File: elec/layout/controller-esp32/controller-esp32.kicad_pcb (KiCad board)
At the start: 2 copper layers, 40 x 40 mm, 0 parts

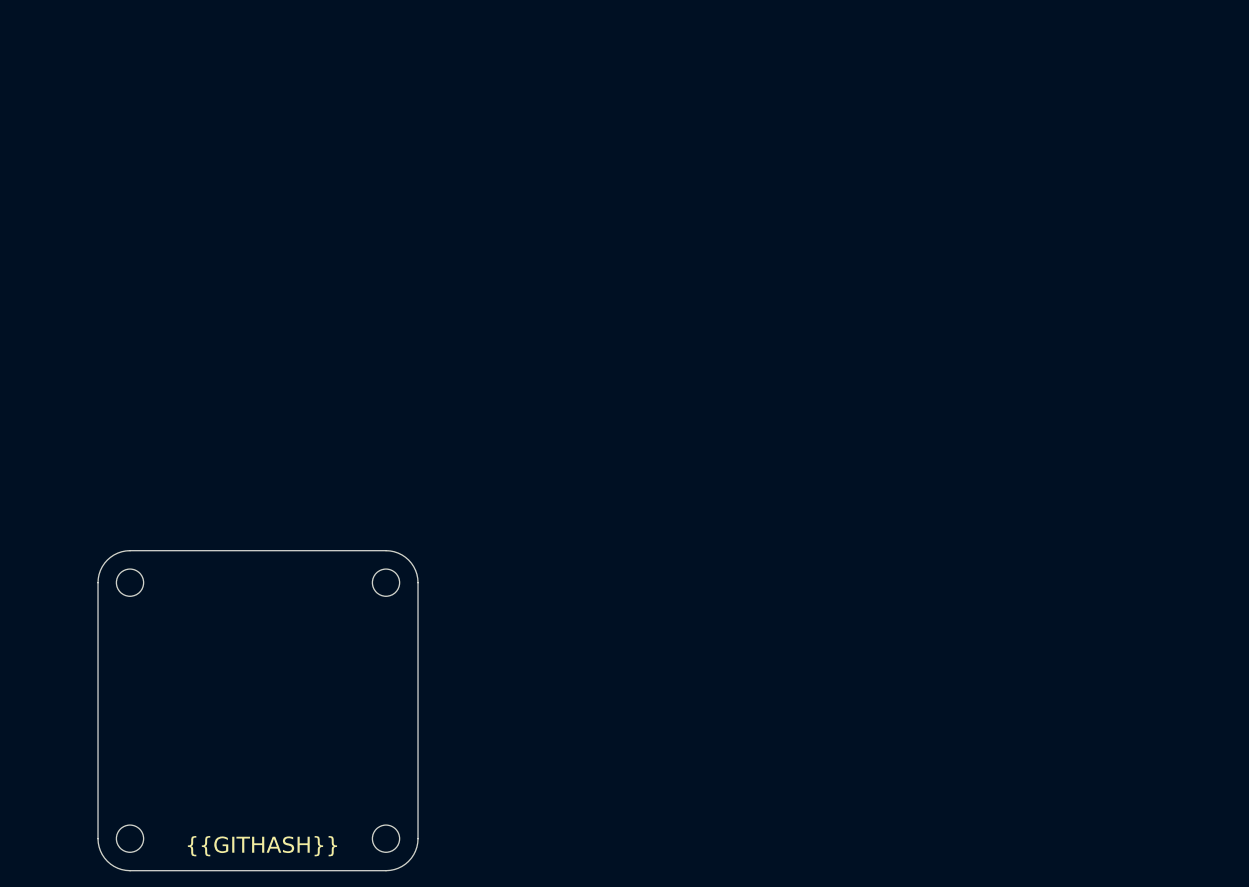
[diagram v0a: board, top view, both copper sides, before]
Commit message: Layout controller block
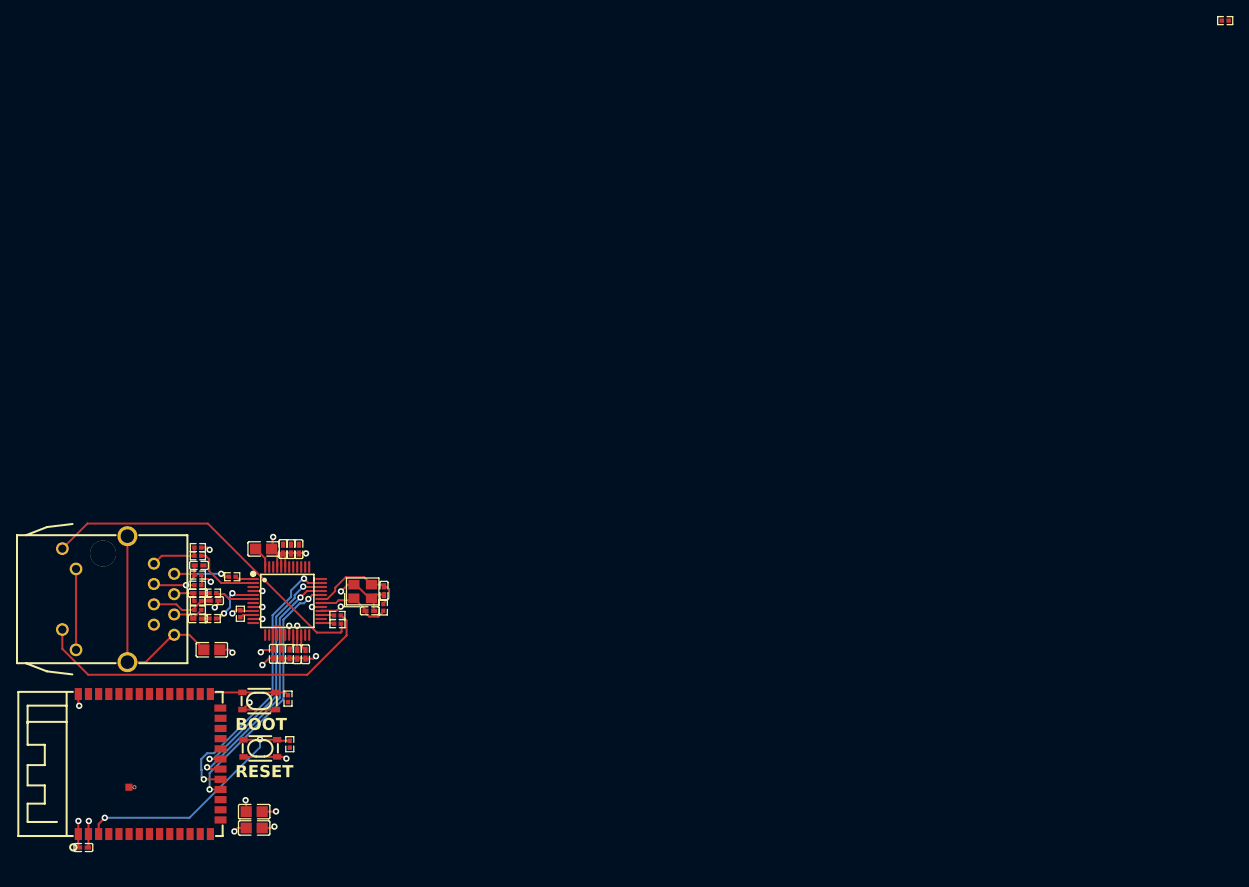
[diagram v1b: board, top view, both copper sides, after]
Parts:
- added U1: 10nF ±10% 50V X7R, atopile:C0402-b3ef17, F.Cu at (155.3, 91.1)
- added U10: 12.4kΩ ±1% 62.5mW, atopile:R0402-56259e, F.Cu at (147.1, 86.0)
- added U11: 1nF ±10% 50V X7R, atopile:C0805-3b2e55, F.Cu at (143.6, 90.5)
- added U12: 220Ω ±1% 62.5mW, atopile:R0402-56259e, F.Cu at (159.3, 87.2)
- added U13: 1MΩ ±1% 62.5mW, atopile:R0402-56259e, F.Cu at (165.0, 85.2)
- added U14: , lib:CRYSTAL-SMD_4P-L3.2-W2.5-BL, F.Cu at (162.4, 83.2)
- added U15: 10pF ±5% 50V C0G, atopile:C0402-b3ef17, F.Cu at (163.3, 85.6)
- added U16: 10pF ±5% 50V C0G, atopile:C0402-b3ef17, F.Cu at (165.1, 83.1)
- added U17: 100Ω ±1% 62.5mW, atopile:R0402-56259e, F.Cu at (270.2, 11.8)
- added U18: , lib:RJ45-TH_J1B1211CCD, F.Cu at (131.9, 84.2)
- added U19: 10nF ±10% 50V X7R, atopile:C0402-b3ef17, F.Cu at (143.9, 84.4)
- added U2: 220Ω ±1% 62.5mW, atopile:R0402-56259e, F.Cu at (159.3, 86.2)
- added U20: 6.8nF ±10% 50V X7R, atopile:C0402-b3ef17, F.Cu at (141.8, 86.6)
- added U21: 33Ω ±1% 62.5mW, atopile:R0402-56259e, F.Cu at (143.7, 86.6)
- added U22: 49.9Ω ±1% 62.5mW, atopile:R0402-56259e, F.Cu at (141.8, 85.5)
- added U23: 6.8nF ±10% 50V X7R, atopile:C0402-b3ef17, F.Cu at (141.8, 83.4)
- added U24: 33Ω ±1% 62.5mW, atopile:R0402-56259e, F.Cu at (143.7, 83.4)
- added U25: 49.9Ω ±1% 62.5mW, atopile:R0402-56259e, F.Cu at (141.8, 84.4)
- added U26: 4.7µF ±10% 10V X5R, atopile:C0402-b3ef17, F.Cu at (153.3, 91.0)
- added U27: 22nF ±10% 50V X7R, atopile:C0402-b3ef17, F.Cu at (142.0, 80.0)
- added U28: 10Ω ±1% 62.5mW, atopile:R0402-56259e, F.Cu at (141.8, 81.2)
- added U29: 33Ω ±1% 62.5mW, atopile:R0402-56259e, F.Cu at (146.1, 81.4)
- added U3: 10µF ±10% 25V X5R, atopile:C0805-3b2e55, F.Cu at (150.1, 77.9)
- added U30: 49.9Ω ±1% 62.5mW, atopile:R0402-56259e, F.Cu at (141.8, 82.4)
- added U31: 33Ω ±1% 62.5mW, atopile:R0402-56259e, F.Cu at (141.8, 78.7)
- added U32: 49.9Ω ±1% 62.5mW, atopile:R0402-56259e, F.Cu at (141.8, 77.7)
- added U33: , lib:LQFP-48_L7.0-W7.0-P0.50-LS9.0-BL, F.Cu at (153.0, 84.4)
- added U34: 10µF ±10% 25V X5R, atopile:C0805-3b2e55, F.Cu at (148.9, 112.8)
- added U35: 10µF ±10% 25V X5R, atopile:C0805-3b2e55, F.Cu at (148.9, 110.7)
- added U36: , lib:KEY-SMD_4P-L4.2-W3.2-P2.20-LS4.6, F.Cu at (149.6, 102.8)
- added U37: 10kΩ ±1% 62.5mW, atopile:R0402-56259e, F.Cu at (153.3, 102.3)
- added U38: , lib:WIRELM-SMD_ESP32-S3-WROOM-1, F.Cu at (135.8, 104.8)
- added U39: 100nF ±10% 16V X7R, atopile:C0402-b3ef17, F.Cu at (127.5, 115.2)
- added U4: 100nF ±10% 16V X7R, atopile:C0402-b3ef17, F.Cu at (153.5, 77.9)
- added U40: , lib:KEY-SMD_4P-L4.2-W3.2-P2.20-LS4.6, F.Cu at (149.5, 96.9)
- added U41: 10kΩ ±1% 62.5mW, atopile:R0402-56259e, F.Cu at (153.1, 96.6)
- added U5: 100nF ±10% 16V X7R, atopile:C0402-b3ef17, F.Cu at (151.3, 91.0)
- added U6: 100nF ±10% 16V X7R, atopile:C0402-b3ef17, F.Cu at (152.3, 91.0)
- added U7: 100nF ±10% 16V X7R, atopile:C0402-b3ef17, F.Cu at (154.5, 77.9)
- added U8: 100nF ±10% 16V X7R, atopile:C0402-b3ef17, F.Cu at (152.5, 77.9)
- added U9: 100nF ±10% 16V X7R, atopile:C0402-b3ef17, F.Cu at (154.3, 91.1)
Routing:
- net hv: track 0.00 -> 51.9 mm, vias 0 -> 13
- net gnd: track 0.00 -> 45.3 mm, vias 0 -> 14
- net RLED_minus: track 0.00 -> 44.2 mm
- net LLED_minus: track 0.00 -> 42.9 mm
- net mosi: track 0.00 -> 35.6 mm, vias 0 -> 2
- net cs: track 0.00 -> 32.4 mm, vias 0 -> 2
- net in: track 0.00 -> 32.2 mm, vias 0 -> 2
- net sck: track 0.00 -> 31.0 mm, vias 0 -> 2
- net miso: track 0.00 -> 30.3 mm, vias 0 -> 2
- net CGND: track 0.00 -> 27.5 mm
- net xout: track 0.00 -> 12.5 mm
- net TD_minus: track 0.00 -> 11.0 mm, vias 0 -> 2
- net in-1: track 0.00 -> 9.92 mm
- net xin: track 0.00 -> 9.44 mm
- net TXP: track 0.00 -> 8.75 mm
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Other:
- board outline removed
- board text added: "BOOT"
- board text added: "RESET"
- board text removed: "{{GITHASH}}"
